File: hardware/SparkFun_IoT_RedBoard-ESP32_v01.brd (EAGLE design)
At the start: 68.6 x 58.4 mm, 213 parts, among them J1 5.5x2.1mm Barrel, J13 QWIIC_RIGHT_ANGLE, J15 MICRO-SD-PUSH-PUSH-EXT-PIN, J2 USB C, J3 USB_SOLDER_PADS, J5 M10NO_SILK, Q1 MBT3904DW1T1, Q11 20V/4.2A/52mΩ/1.4W, Q13 20V/4.2A/52mΩ/1.4W, Q3 20V/4.2A/52mΩ/1.4W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

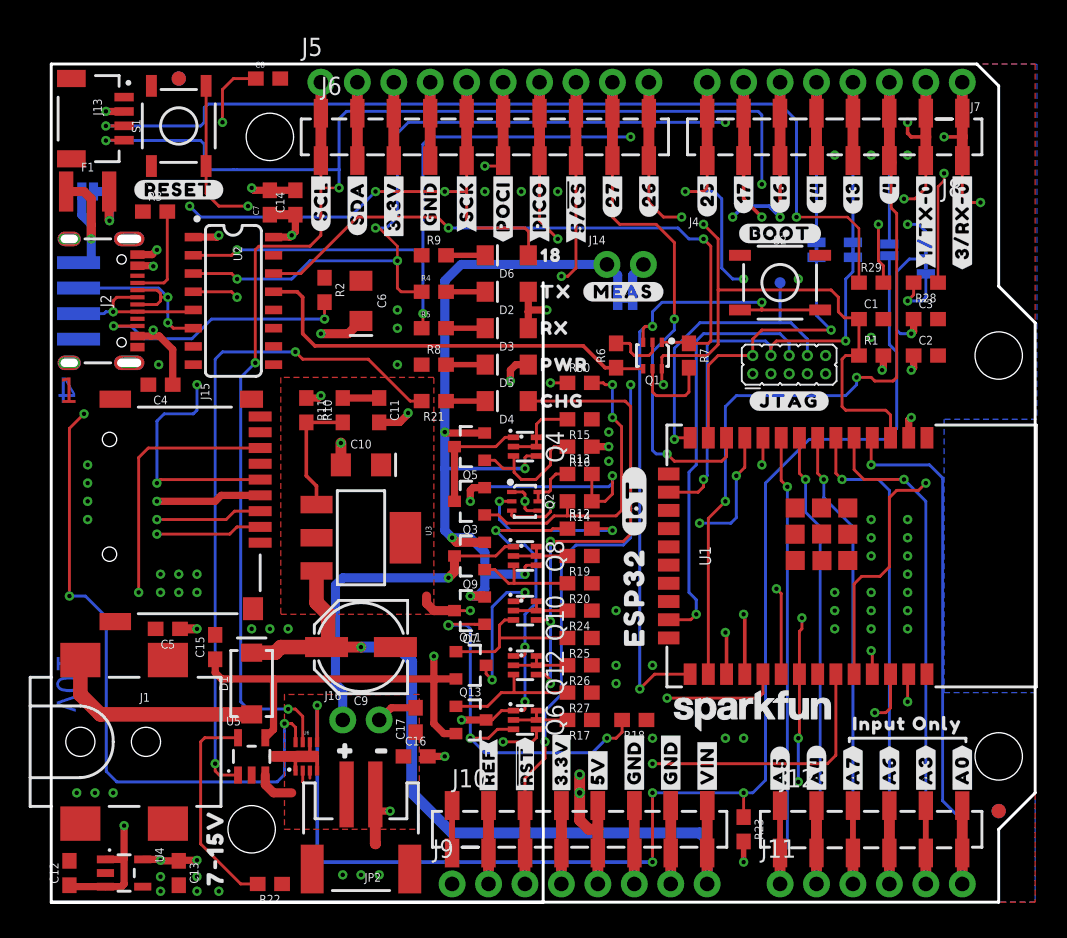
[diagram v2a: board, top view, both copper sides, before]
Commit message: Adjust LED jumper
New position allows better label placement
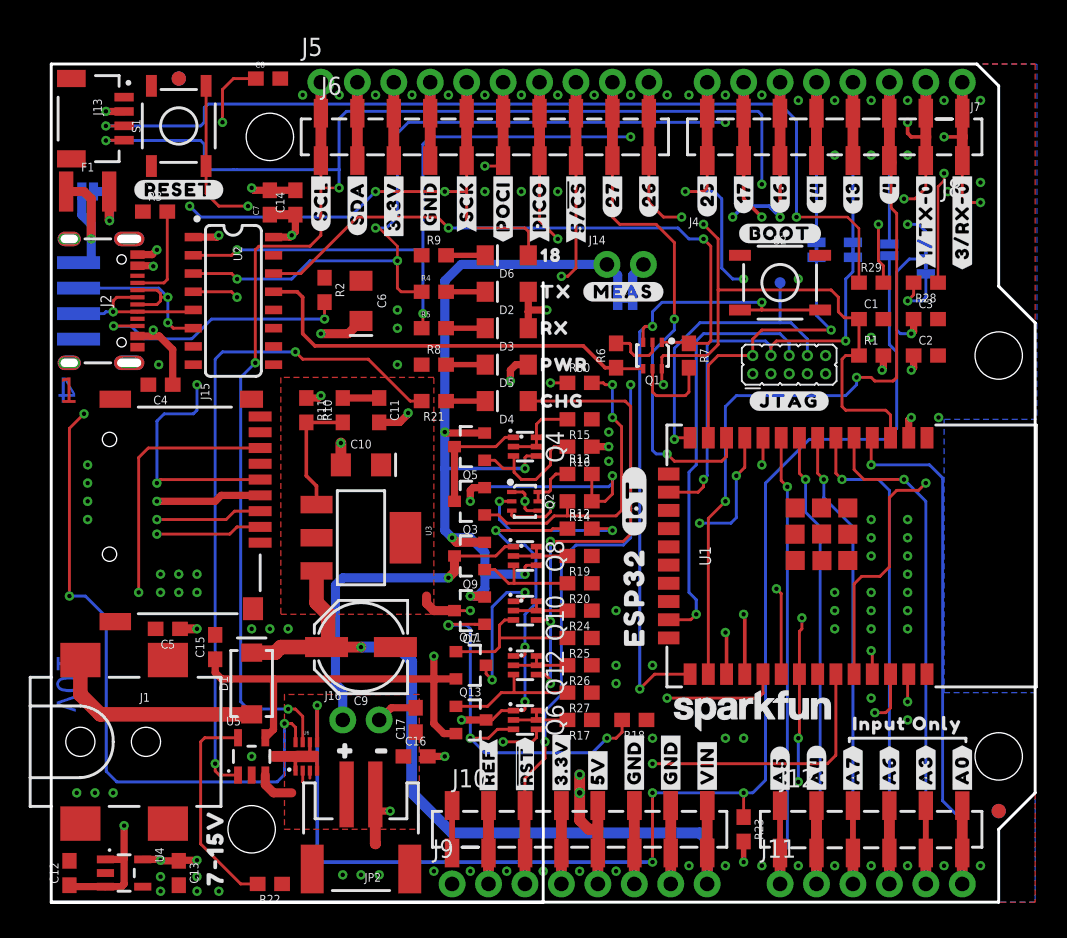
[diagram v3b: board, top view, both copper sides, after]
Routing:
- net GND: vias 70 -> 111
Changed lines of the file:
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@@
 <drawing>
 <settings>
-<setting alwaysvectorfont="yes"/>
+<setting alwaysvectorfont="no"/>
 <setting keepoldvectorfont="yes"/>
 <setting verticaltext="up"/>
@@
 <layers>
 <layer number="1" name="Top" color="4" fill="1" visible="yes" active="yes"/>
-<layer number="2" name="Route2" color="24" fill="1" visible="no" active="yes"/>
-<layer number="15" name="Route15" color="23" fill="1" visible="no" active="yes"/>
+<layer number="2" name="Route2" color="24" fill="1" visible="yes" active="yes"/>
+<layer number="15" name="Route15" color="23" fill="1" visible="yes" active="yes"/>
 <layer number="16" name="Bottom" color="1" fill="1" visible="yes" active="yes"/>
 <layer number="17" name="Pads" color="2" fill="1" visible="yes" active="yes"/>
@@
 <layer number="19" name="Unrouted" color="6" fill="1" visible="yes" active="yes"/>
 <layer number="20" name="Dimension" color="24" fill="1" visible="yes" active="yes"/>
-<layer number="21" name="tPlace" color="16" fill="1" visible="yes" active="yes"/>
-<layer number="22" name="bPlace" color="14" fill="1" visible="yes" active="yes"/>
+<layer number="21" name="tPlace" color="16" fill="1" visible="no" active="yes"/>
+<layer number="22" name="bPlace" color="14" fill="1" visible="no" active="yes"/>
 <layer number="23" name="tOrigins" color="15" fill="1" visible="yes" active="yes"/>
 <layer number="24" name="bOrigins" color="15" fill="1" visible="yes" active="yes"/>
@@
 <wire x1="14.136" y1="49.618" x2="13.97" y2="49.784" width="0.508" layer="1"/>
 <via x="13.97" y="49.784" extent="1-16" drill="0.3048"/>
+<via x="62.23" y="2.54" extent="1-16" drill="0.3048"/>
+<via x="59.69" y="2.54" extent="1-16" drill="0.3048"/>
+<via x="57.15" y="2.54" extent="1-16" drill="0.3048"/>
+<via x="54.61" y="2.54" extent="1-16" drill="0.3048"/>
+<via x="52.07" y="2.54" extent="1-16" drill="0.3048"/>
+<via x="64.77" y="2.54" extent="1-16" drill="0.3048"/>
+<via x="49.53" y="2.54" extent="1-16" drill="0.3048"/>
+<via x="46.99" y="2.54" extent="1-16" drill="0.3048"/>
+<via x="44.45" y="2.54" extent="1-16" drill="0.3048"/>
+<via x="62.23" y="55.88" extent="1-16" drill="0.3048"/>
+<via x="59.69" y="55.88" extent="1-16" drill="0.3048"/>
+<via x="57.15" y="55.88" extent="1-16" drill="0.3048"/>
+<via x="54.61" y="55.88" extent="1-16" drill="0.3048"/>
+<via x="52.07" y="55.88" extent="1-16" drill="0.3048"/>
+<via x="64.77" y="55.88" extent="1-16" drill="0.3048"/>
+<via x="64.77" y="50.165" extent="1-16" drill="0.3048"/>
+<via x="62.484" y="49.53" extent="1-16" drill="0.3048"/>
+<via x="39.37" y="2.159" extent="1-16" drill="0.3048"/>
+<via x="36.83" y="2.159" extent="1-16" drill="0.3048"/>
+<via x="34.29" y="2.159" extent="1-16" drill="0.3048"/>
+<via x="31.75" y="2.159" extent="1-16" drill="0.3048"/>
+<via x="29.21" y="2.159" extent="1-16" drill="0.3048"/>
+<via x="26.67" y="2.159" extent="1-16" drill="0.3048"/>
+<via x="49.53" y="56.261" extent="1-16" drill="0.3048"/>
+<via x="46.99" y="56.261" extent="1-16" drill="0.3048"/>
+<via x="44.45" y="56.261" extent="1-16" drill="0.3048"/>
+<via x="40.386" y="56.261" extent="1-16" drill="0.3048"/>
+<via x="42.926" y="56.261" extent="1-16" drill="0.3048"/>
+<via x="37.846" y="56.261" extent="1-16" drill="0.3048"/>
+<via x="35.306" y="56.261" extent="1-16" drill="0.3048"/>
+<via x="32.766" y="56.261" extent="1-16" drill="0.3048"/>
+<via x="30.226" y="56.261" extent="1-16" drill="0.3048"/>
+<via x="27.686" y="56.261" extent="1-16" drill="0.3048"/>
+<via x="25.146" y="56.261" extent="1-16" drill="0.3048"/>
+<via x="22.606" y="56.261" extent="1-16" drill="0.3048"/>
+<via x="20.066" y="56.261" extent="1-16" drill="0.3048"/>
+<via x="17.526" y="56.261" extent="1-16" drill="0.3048"/>
+<via x="13.97" y="10.16" extent="1-16" drill="0.3048"/>
+<via x="61.849" y="33.782" extent="1-16" drill="0.3048"/>
+<via x="59.69" y="12.7" extent="1-16" drill="0.3048"/>
+<via x="57.15" y="14.224" extent="1-16" drill="0.3048"/>
 </signal>
 <signal name="VIN" class="1">

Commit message: Improve GND continuity
Add several GND vias
Adjust some traces to allow GND to pour through
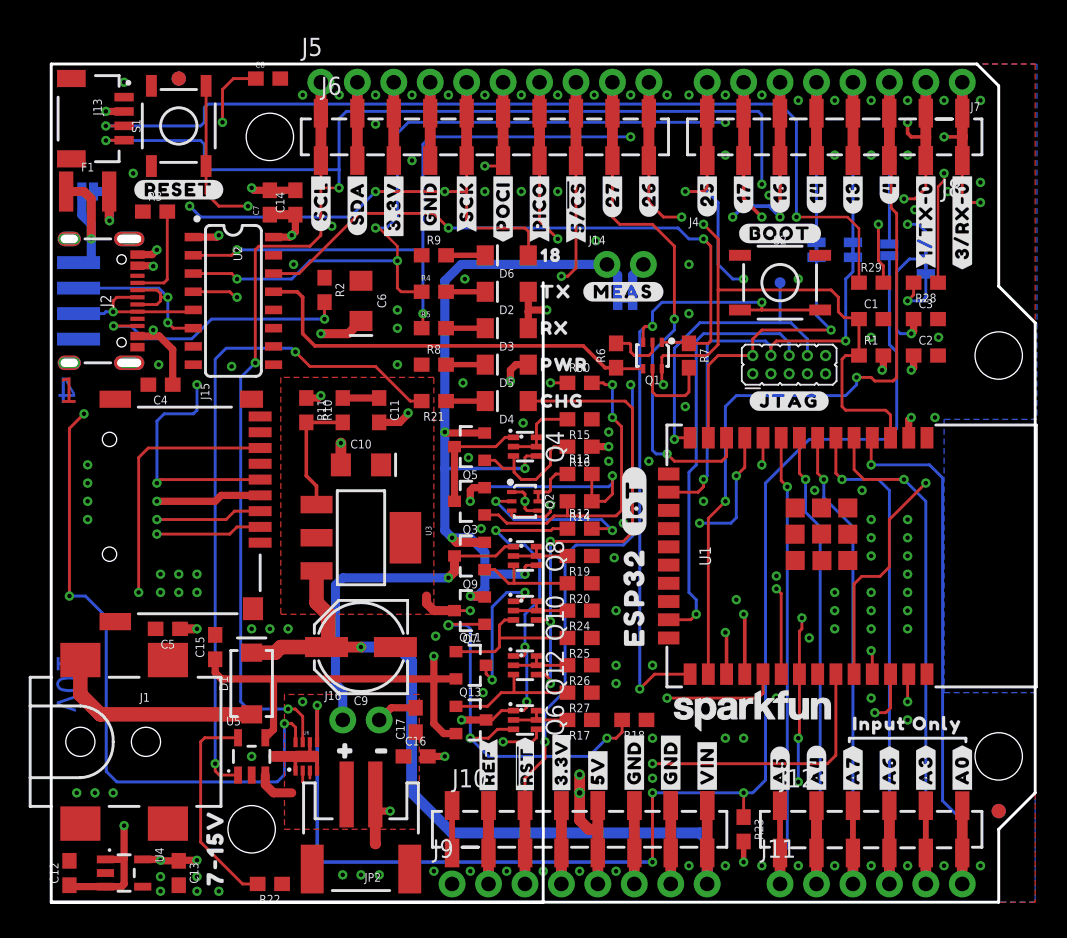
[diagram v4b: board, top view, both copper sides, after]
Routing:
- net ESP32_RXD0: track 116.1 -> 115.2 mm
- net GND: vias 111 -> 145

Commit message: Add "revised by" and change version number
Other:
- board text added: "Revised by: Dryw Wade"
- board text added: "v02"
- board text removed: "v01"
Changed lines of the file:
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@@
 <wire x1="55.626" y1="11.43" x2="63.754" y2="11.43" width="0.2032" layer="21"/>
 <wire x1="63.754" y1="11.43" x2="63.754" y2="11.176" width="0.2032" layer="21"/>
-<text x="1.27" y="15.24" size="1.778" layer="16" font="vector" ratio="15" rot="MR270" align="center">v01</text>
+<text x="1.27" y="15.24" size="1.778" layer="16" font="vector" ratio="15" rot="MR270" align="center">v02</text>
 <text x="78.74" y="43.18" size="1.778" layer="51" font="vector" ratio="10">- Board thickness is 1.6mm</text>
 <text x="78.74" y="38.1" size="1.778" layer="51" font="vector" ratio="10">- No clean process</text>
@@
 <text x="1.778" y="34.798" size="1.778" layer="16" font="vector" ratio="15" rot="MR0">4</text>
 <text x="0.508" y="34.798" size="1.778" layer="1" font="vector" ratio="15">1</text>
+<text x="30.861" y="-43.688" size="1.778" layer="51">Revised by: Dryw Wade</text>
 </plain>
 <attributes>

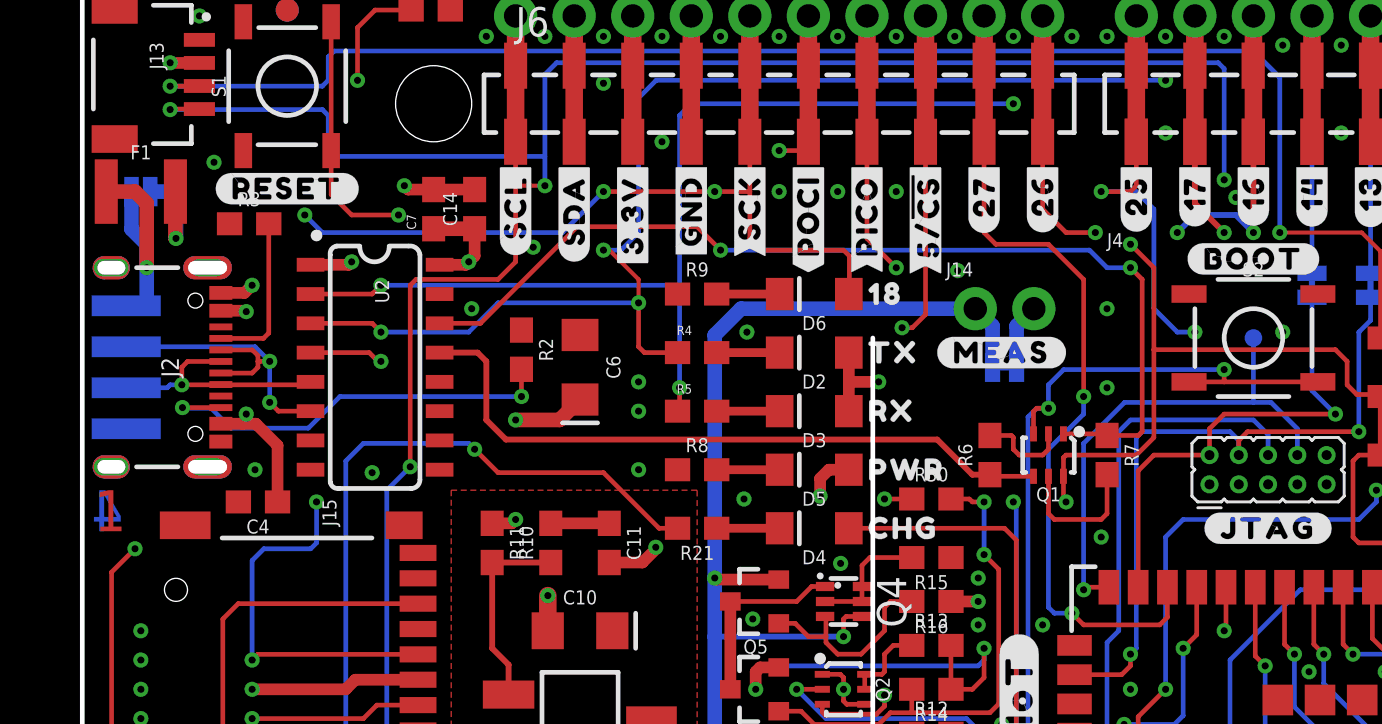
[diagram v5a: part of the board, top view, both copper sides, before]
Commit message: Change PTC Fuse
Reduce current rating of PTC
Move PTC to 5V_MEAS to protect all power inputs rather than just USB
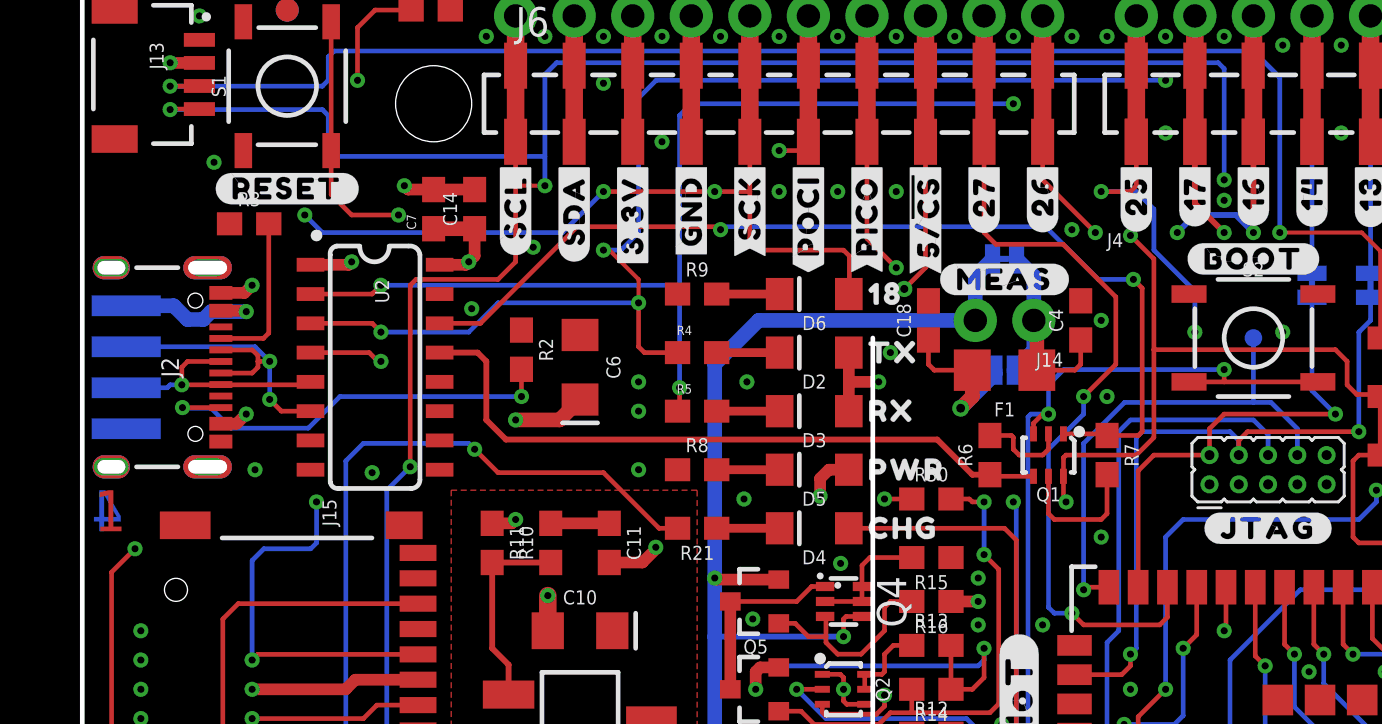
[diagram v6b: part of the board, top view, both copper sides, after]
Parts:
- removed U$81: (no value), output-ESP32:#MEAS#1851
- removed U$82: (no value), output-ESP32:#BYP#35
- added C18: 0.1uF, SparkFun-Capacitors:0603
- added U$11: (no value), output:#MEAS#0
- added U$64: (no value), output:#BYP#0
- F1: value 6V/2A -> 6V/0.75A; device SparkFun-Fuses:1210 -> SparkFun-Fuses:1206
- moved BYP 38.3 mm to (40.0, 41.8), turned to 0 degrees
- moved F1 38.3 mm to (40.0, 41.8), turned to 180 degrees
- moved C4 36.5 mm to (43.3, 43.9), turned to 90 degrees
- moved JP10 4.70 mm to (40.0, 46.6)
- moved U$42 3.18 mm to (40.0, 45.7)
- moved J14 2.59 mm to (41.3, 43.9), turned to 180 degrees
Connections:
- removed net VBUS: BYP.1, C4.1, F1.1, J2.VBUS1, J2.VBUS2, J3.VBUS
- new net N$19: BYP.1, C4.1, F1.1, J14.1, JP10.2
- net 5V: now also BYP.2, C18.1, F1.2; no longer J14.2, JP10.2
- net 5V_MEAS: now also J14.2; no longer J14.1
- net GND: now also C18.2
- net V_USB: now also J2.VBUS1, J2.VBUS2, J3.VBUS; no longer BYP.2, F1.2
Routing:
- net VBUS: track 28.8 -> 0.00 mm, vias 3 -> 0
- net N$19: track 0.00 -> 10.8 mm
- net ESP32_GPIO5_!CS!: track 114.8 -> 111.4 mm
- net V_USB: track 121.0 -> 118.5 mm, vias 7 -> 8
- net 5V: track 94.9 -> 92.4 mm, vias 3 -> 4
- net ESP32_GPIO27: track 36.3 -> 37.9 mm
- net 5V_MEAS: track 72.0 -> 71.1 mm
- net ESP32_GPIO26: track 41.9 -> 41.2 mm
- net GND: vias 145 -> 146
